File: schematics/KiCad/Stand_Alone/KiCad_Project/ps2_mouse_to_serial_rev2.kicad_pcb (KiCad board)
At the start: 2 copper layers, 91.4 x 71.1 mm, 28 parts, among them J1 Barrel Jack 2.1 mm, J2 DB9 Female, J3 Mini-DIN-6, Q1 BC547, SW1 1C2P, U1 74LS00, U2 L7805, U3 L78L05

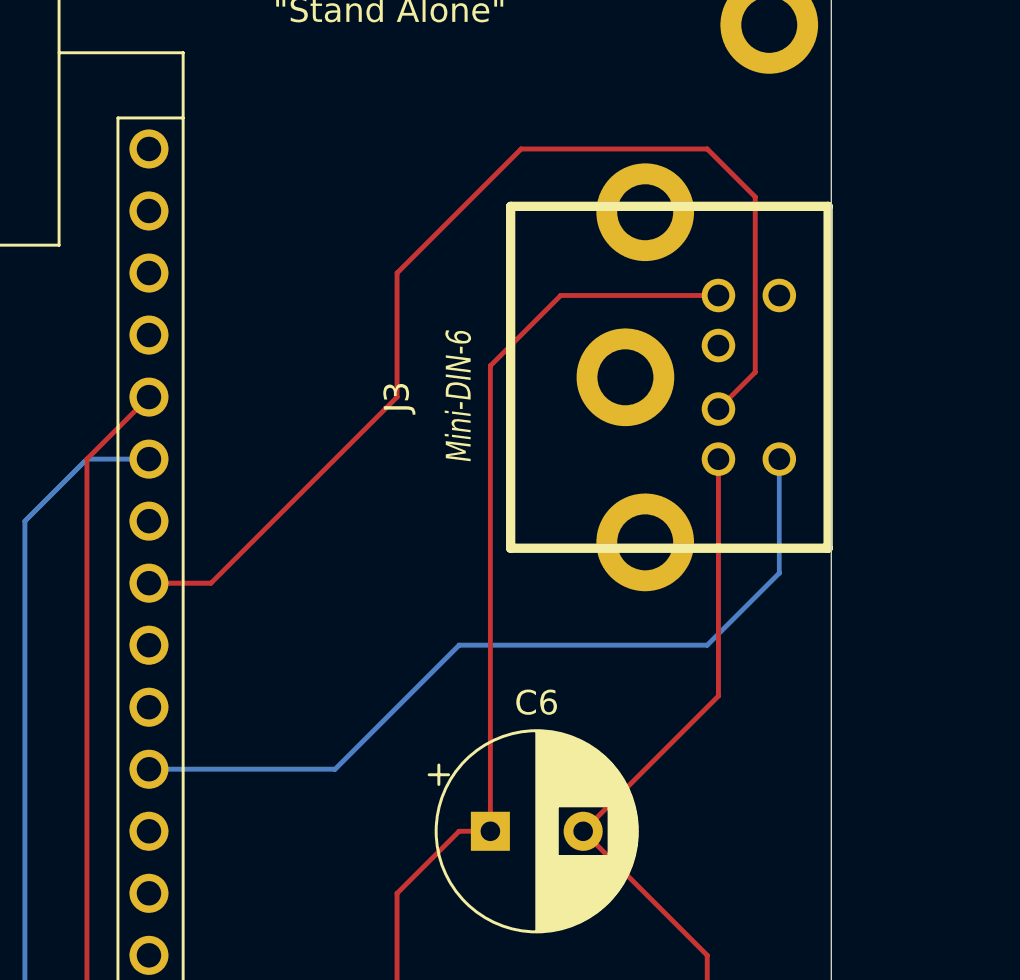
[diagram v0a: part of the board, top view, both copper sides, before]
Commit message: V1.0.1-rev2.1
- Corregido un error en la colocación del conector PS/2 en la placa "Stand Alone" del proyecto KiCad.
- Recordar que aún no he podido producir físicamente estas placas, por lo que si vais a producirlas, revisar el proyecto 3 veces en búsqueda de errores.
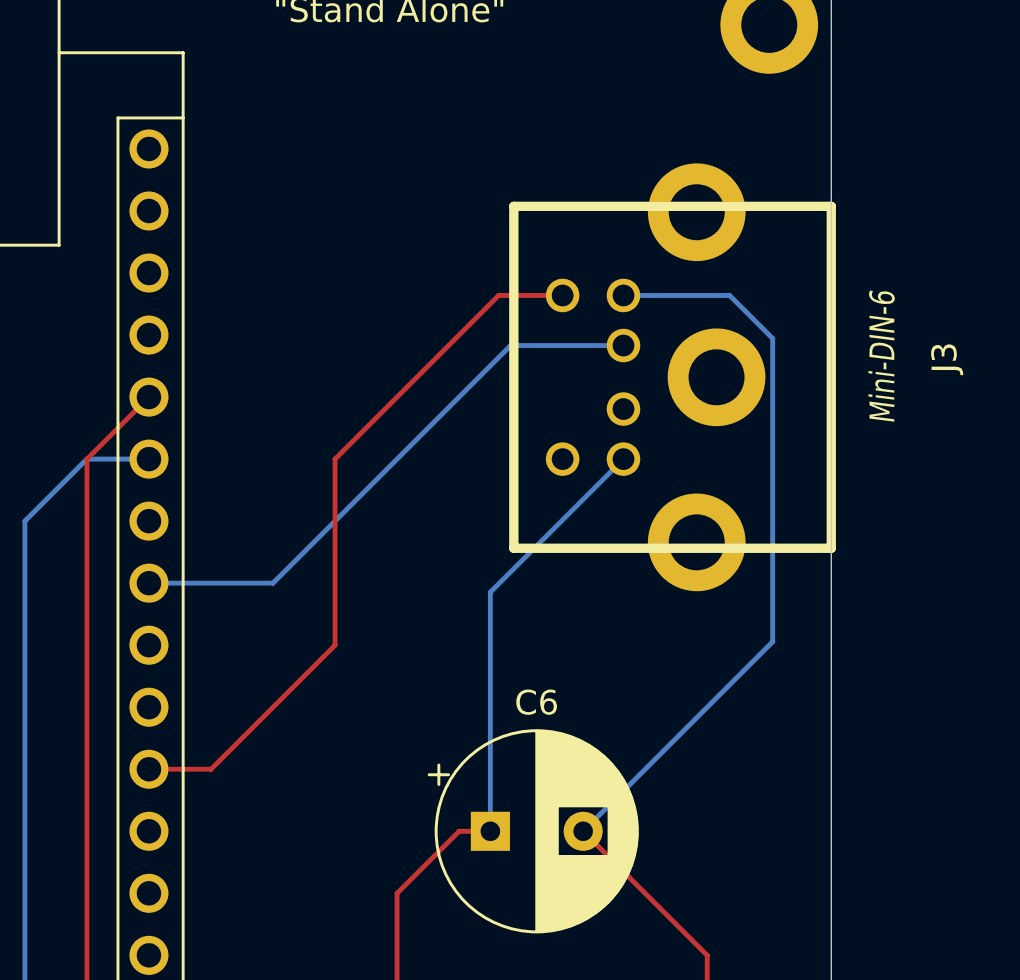
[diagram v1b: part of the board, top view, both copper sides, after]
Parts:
- moved J3 13.1 mm to (116.8, 42.4), turned to -90 degrees
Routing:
- net Net-(A1-D5): track 45.3 -> 23.5 mm
- net Net-(D2-K): track 255.3 -> 268.0 mm
- net Net-(A1-VIN): track 139.3 -> 127.3 mm
- net Net-(A1-D2): track 33.8 -> 29.4 mm
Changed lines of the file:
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@@
   )
   (footprint "CustomFootPrints:Conn_Mini_DIN_6pin" (layer "F.Cu")
-    (at 103.71074 42.36974 90)
+    (at 116.84 42.36974 -90)
     (descr "Mini-DIN Connector 6 pin")
     (tags "MINI DIN CONN 6PIN")
@@
     (fp_line (start 7.00024 12.99972) (end -7.00024 12.99972)
       (stroke (width 0.381) (type solid)) (layer "F.SilkS"))
-    (pad "1" thru_hole circle (at -1.30048 8.509 270) (size 1.3716 1.3716) (drill 0.889) (layers "*.Cu" "*.Mask" "F.SilkS")
+    (pad "1" thru_hole circle (at -1.30048 8.509 90) (size 1.3716 1.3716) (drill 0.889) (layers "*.Cu" "*.Mask" "F.SilkS")
       (net 22 "Net-(A1-D5)") (pintype "passive"))
-    (pad "2" thru_hole circle (at 1.30048 8.509 270) (size 1.3716 1.3716) (drill 0.889) (layers "*.Cu" "*.Mask" "F.SilkS")
+    (pad "2" thru_hole circle (at 1.30048 8.509 90) (size 1.3716 1.3716) (drill 0.889) (layers "*.Cu" "*.Mask" "F.SilkS")
       (net 42 "unconnected-(J3-Pad2)") (pintype "passive+no_connect"))
-    (pad "3" thru_hole circle (at -3.35026 8.509 270) (size 1.3716 1.3716) (drill 0.889) (layers "*.Cu" "*.Mask" "F.SilkS")
+    (pad "3" thru_hole circle (at -3.35026 8.509 90) (size 1.3716 1.3716) (drill 0.889) (layers "*.Cu" "*.Mask" "F.SilkS")
       (net 7 "Net-(D2-K)") (pintype "passive"))
-    (pad "4" thru_hole circle (at 3.35026 8.509 270) (size 1.3716 1.3716) (drill 0.889) (layers "*.Cu" "*.Mask" "F.SilkS")
+    (pad "4" thru_hole circle (at 3.35026 8.509 90) (size 1.3716 1.3716) (drill 0.889) (layers "*.Cu" "*.Mask" "F.SilkS")
       (net 3 "Net-(A1-VIN)") (pintype "passive"))
-    (pad "5" thru_hole circle (at -3.35026 11.00074 270) (size 1.3716 1.3716) (drill 0.889) (layers "*.Cu" "*.Mask" "F.SilkS")
+    (pad "5" thru_hole circle (at -3.35026 11.00074 90) (size 1.3716 1.3716) (drill 0.889) (layers "*.Cu" "*.Mask" "F.SilkS")
       (net 19 "Net-(A1-D2)") (pintype "passive"))
-    (pad "6" thru_hole circle (at 3.35026 11.00074 270) (size 1.3716 1.3716) (drill 0.889) (layers "*.Cu" "*.Mask" "F.SilkS")
+    (pad "6" thru_hole circle (at 3.35026 11.00074 90) (size 1.3716 1.3716) (drill 0.889) (layers "*.Cu" "*.Mask" "F.SilkS")
       (net 43 "unconnected-(J3-Pad6)") (pintype "passive+no_connect"))
-    (pad "GND" thru_hole circle (at -6.75894 5.50926 270) (size 4.0005 4.0005) (drill 2.29108) (layers "*.Cu" "*.SilkS" "*.Mask"))
-    (pad "GND" thru_hole circle (at 0 4.699 270) (size 4.0005 4.0005) (drill 2.29108) (layers "*.Cu" "*.SilkS" "*.Mask"))
-    (pad "GND" thru_hole circle (at 6.75894 5.50926 270) (size 4.0005 4.0005) (drill 2.29108) (layers "*.Cu" "*.SilkS" "*.Mask"))
+    (pad "GND" thru_hole circle (at -6.75894 5.50926 90) (size 4.0005 4.0005) (drill 2.29108) (layers "*.Cu" "*.SilkS" "*.Mask"))
+    (pad "GND" thru_hole circle (at 0 4.699 90) (size 4.0005 4.0005) (drill 2.29108) (layers "*.Cu" "*.SilkS" "*.Mask"))
+    (pad "GND" thru_hole circle (at 6.75894 5.50926 90) (size 4.0005 4.0005) (drill 2.29108) (layers "*.Cu" "*.SilkS" "*.Mask"))
     (model "r_mini_dins/minidin_6.wrl"
       (offset (xyz 0 0 0))
@@
   (segment (start 78.74 86.36) (end 73.66 86.36) (width 0.2) (layer "F.Cu") (net 3))
   (segment (start 87.62 86.36) (end 88.9 87.64) (width 0.2) (layer "F.Cu") (net 3))
-  (segment (start 112.21974 39.01948) (end 105.76052 39.01948) (width 0.2) (layer "F.Cu") (net 3))
-  (segment (start 105.76052 39.01948) (end 102.88 41.9) (width 0.2) (layer "F.Cu") (net 3))
   (segment (start 78.74 86.36) (end 87.62 86.36) (width 0.2) (layer "F.Cu") (net 3))
   (segment (start 78.74 73.66) (end 73.66 68.58) (width 0.2) (layer "F.Cu") (net 3))
@@
   (segment (start 63.5 63.5) (end 68.58 68.58) (width 0.2) (layer "F.Cu") (net 3))
   (segment (start 88.9 87.64) (end 91.43 87.64) (width 0.2) (layer "F.Cu") (net 3))
-  (segment (start 102.88 41.9) (end 102.88 60.96) (width 0.2) (layer "F.Cu") (net 3))
   (segment (start 102.88 60.96) (end 101.6 60.96) (width 0.2) (layer "F.Cu") (net 3))
   (segment (start 60.96 48.26) (end 60.96 55.8) (width 0.2) (layer "F.Cu") (net 3))
+  (segment (start 102.88 60.96) (end 102.88 51.171) (width 0.2) (layer "B.Cu") (net 3))
+  (segment (start 102.88 51.171) (end 108.331 45.72) (width 0.2) (layer "B.Cu") (net 3))
   (segment (start 102.87 83.82) (end 109.22 83.82) (width 0.2) (layer "F.Cu") (net 4))
   (segment (start 58.42 60.96) (end 58.42 71.12) (width 0.2) (layer "F.Cu") (net 5))
@@
   (segment (start 111.76 76.2) (end 111.76 83.82) (width 0.2) (layer "F.Cu") (net 7))
   (segment (start 109.22 91.44) (end 111.76 88.9) (width 0.2) (layer "F.Cu") (net 7))
-  (segment (start 112.21974 55.42026) (end 106.68 60.96) (width 0.2) (layer "F.Cu") (net 7))
   (segment (start 52.07 34.29) (end 48.26 34.29) (width 0.2) (layer "F.Cu") (net 7))
   (segment (start 55.88 76.2) (end 53.34 78.74) (width 0.2) (layer "F.Cu") (net 7))
@@
   (segment (start 53.26 91.44) (end 53.34 91.36) (width 0.2) (layer "F.Cu") (net 7))
   (segment (start 30.48 91.44) (end 43.18 91.44) (width 0.2) (layer "F.Cu") (net 7))
-  (segment (start 112.21974 45.72) (end 112.21974 55.42026) (width 0.2) (layer "F.Cu") (net 7))
   (segment (start 111.76 88.9) (end 111.76 83.82) (width 0.2) (layer "F.Cu") (net 7))
   (segment (start 33.520331 42.73) (end 41.46 42.73) (width 0.2) (layer "F.Cu") (net 7))
@@
   (segment (start 53.34 91.36) (end 58.34 91.36) (width 0.2) (layer "F.Cu") (net 7))
   (segment (start 63.5 60.96) (end 55.88 60.96) (width 0.2) (layer "B.Cu") (net 7))
+  (segment (start 114.44125 40.78125) (end 112.67948 39.01948) (width 0.2) (layer "B.Cu") (net 7))
   (segment (start 55.88 81.28) (end 53.34 78.74) (width 0.2) (layer "B.Cu") (net 7))
   (segment (start 73.66 66.04) (end 68.58 66.04) (width 0.2) (layer "B.Cu") (net 7))
   (segment (start 68.58 66.04) (end 63.5 60.96) (width 0.2) (layer "B.Cu") (net 7))
   (segment (start 55.8 88.9) (end 55.88 88.9) (width 0.2) (layer "B.Cu") (net 7))
+  (segment (start 112.67948 39.01948) (end 108.331 39.01948) (width 0.2) (layer "B.Cu") (net 7))
+  (segment (start 106.68 60.96) (end 114.44125 53.19875) (width 0.2) (layer "B.Cu") (net 7))
   (segment (start 55.88 88.9) (end 55.88 81.28) (width 0.2) (layer "B.Cu") (net 7))
   (segment (start 53.34 91.36) (end 55.8 88.9) (width 0.2) (layer "B.Cu") (net 7))
+  (segment (start 114.44125 53.19875) (end 114.44125 40.78125) (width 0.2) (layer "B.Cu") (net 7))
   (segment (start 55.88 60.96) (end 53.34 58.42) (width 0.2) (layer "B.Cu") (net 7))
   (segment (start 58.42 35.56) (end 48.26 35.56) (width 0.2) (layer "F.Cu") (net 8))
@@
   (segment (start 83.82 76.2) (end 81.28 78.74) (width 0.2) (layer "B.Cu") (net 15))
   (segment (start 81.28 78.74) (end 60.96 78.74) (width 0.2) (layer "B.Cu") (net 15))
-  (segment (start 88.9 58.42) (end 96.52 58.42) (width 0.2) (layer "B.Cu") (net 19))
-  (segment (start 111.76 53.34) (end 114.71148 50.38852) (width 0.2) (layer "B.Cu") (net 19))
-  (segment (start 96.52 58.42) (end 101.6 53.34) (width 0.2) (layer "B.Cu") (net 19))
-  (segment (start 101.6 53.34) (end 111.76 53.34) (width 0.2) (layer "B.Cu") (net 19))
-  (segment (start 114.71148 50.38852) (end 114.71148 45.72) (width 0.2) (layer "B.Cu") (net 19))
-  (segment (start 99.06 38.1) (end 99.06 43.18) (width 0.2) (layer "F.Cu") (net 22))
-  (segment (start 104.14 33.02) (end 99.06 38.1) (width 0.2) (layer "F.Cu") (net 22))
-  (segment (start 113.72568 42.16428) (end 113.72568 34.98568) (width 0.2) (layer "F.Cu") (net 22))
-  (segment (start 112.21974 43.67022) (end 113.72568 42.16428) (width 0.2) (layer "F.Cu") (net 22))
-  (segment (start 111.76 33.02) (end 104.14 33.02) (width 0.2) (layer "F.Cu") (net 22))
-  (segment (start 99.06 43.18) (end 91.44 50.8) (width 0.2) (layer "F.Cu") (net 22))
-  (segment (start 91.44 50.8) (end 88.9 50.8) (width 0.2) (layer "F.Cu") (net 22))
-  (segment (start 113.72568 34.98568) (end 111.76 33.02) (width 0.2) (layer "F.Cu") (net 22))
+  (segment (start 91.44 58.42) (end 88.9 58.42) (width 0.2) (layer "F.Cu") (net 19))
+  (segment (start 96.52 53.34) (end 91.44 58.42) (width 0.2) (layer "F.Cu") (net 19))
+  (segment (start 103.22052 39.01948) (end 96.52 45.72) (width 0.2) (layer "F.Cu") (net 19))
+  (segment (start 96.52 45.72) (end 96.52 53.34) (width 0.2) (layer "F.Cu") (net 19))
+  (segment (start 105.83926 39.01948) (end 103.22052 39.01948) (width 0.2) (layer "F.Cu") (net 19))
+  (segment (start 88.9 50.8) (end 93.98 50.8) (width 0.2) (layer "B.Cu") (net 22))
+  (segment (start 93.98 50.8) (end 103.71074 41.06926) (width 0.2) (layer "B.Cu") (net 22))
+  (segment (start 103.71074 41.06926) (end 108.331 41.06926) (width 0.2) (layer "B.Cu") (net 22))
   (segment (start 27.94 43.18) (end 27.94 46.914669) (width 0.2) (layer "F.Cu") (net 41))
   (segment (start 43.18 40.64) (end 30.48 40.64) (width 0.2) (layer "F.Cu") (net 41))
